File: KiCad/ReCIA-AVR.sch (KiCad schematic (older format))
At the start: 11 parts, among them U1 AVR128DA64-I_MR, U2 74AHCT1G17, U3 TLC2932AIPWR, U5 8520_DIP

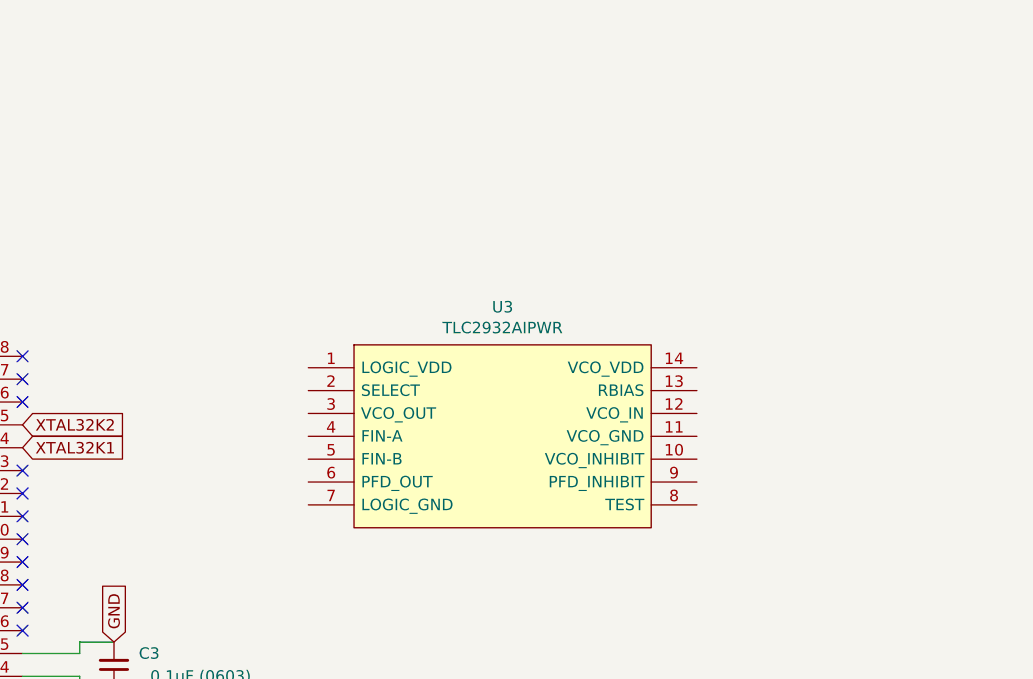
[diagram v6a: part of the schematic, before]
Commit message: Fixed placement of PLL-chip and added inductor and caps for power supply pins Logic VDD and VCO VDD for the AVR-version
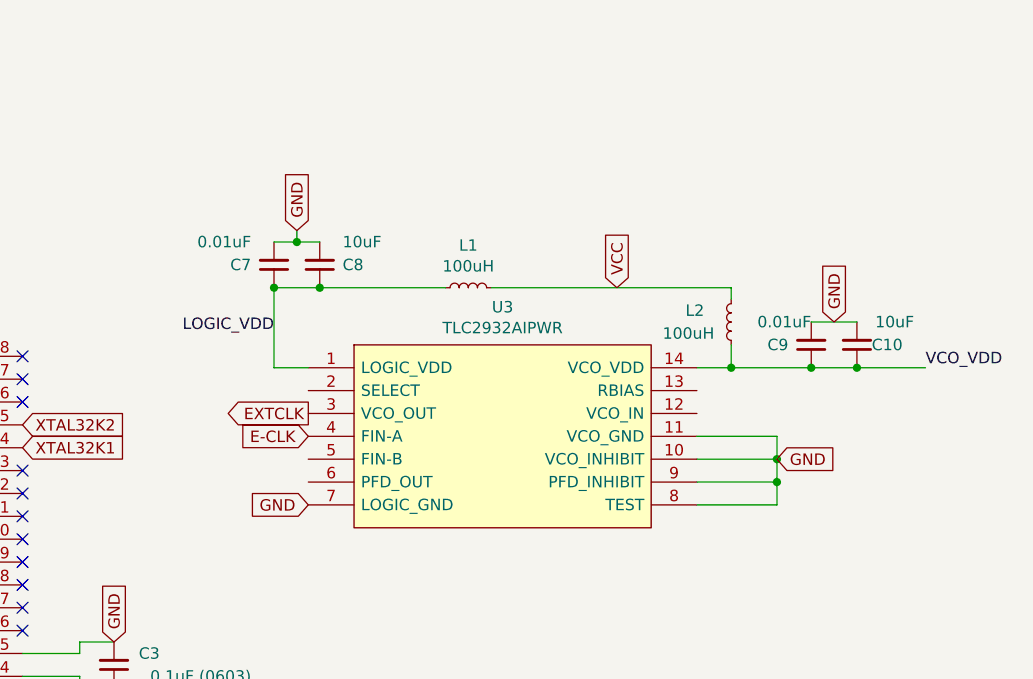
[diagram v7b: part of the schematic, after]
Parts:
- added C10, C8: 10uF, Capacitor_SMD:C_0805_2012Metric_Pad1.18x1.45mm_HandSolder, symbol Device:C_Small
- added C7, C9: 0.01uF, Capacitor_SMD:C_0603_1608Metric_Pad1.08x0.95mm_HandSolder, symbol Device:C_Small
- added L1, L2: 100uH, Inductor_SMD:L_0805_2012Metric_Pad1.15x1.40mm_HandSolder, symbol Device:L_Small
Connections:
- net E-CLK: now also U3.4 (FIN-A)
- net EXTCLK: now also U3.3 (VCO_OUT)
- net GND: now also U3.10 (VCO_INHIBIT), U3.11 (VCO_GND), U3.7 (LOGIC_GND), U3.8 (TEST), U3.9 (PFD_INHIBIT), C10.2, C7.2, C8.2, C9.2
- net VCC: now also L1.2, L2.2
- net LOGIC_VDD: now reaches U3.1 (LOGIC_VDD)
- net LOGIC_VDD: now also C7.1, C8.1, L1.1
- net VCO_VDD: now reaches U3.14 (VCO_VDD)
- net VCO_VDD: now also C10.1, C9.1, L2.1
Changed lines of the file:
@@
 Text GLabel 2050 4600 3    50   Input ~ 0
 GND
+$Comp
+L Device:L_Small L1
+U 1 1 6782C3A7
+P 8550 2350
+F 0 "L1" V 8735 2350 50  0000 C CNN
+F 1 "100uH" V 8644 2350 50  0000 C CNN
+F 2 "Inductor_SMD:L_0805_2012Metric_Pad1.15x1.40mm_HandSolder" H 8550 2350 50  0001 C CNN
+F 3 "~" H 8550 2350 50  0001 C CNN
+	1    8550 2350
+	0    -1   -1   0
+$EndComp
+$Comp
+L Device:L_Small L2
+U 1 1 6782D183
+P 9700 2500
+F 0 "L2" H 9900 2450 50  0000 R CNN
+F 1 "100uH" H 10000 2550 50  0000 R CNN
+F 2 "Inductor_SMD:L_0805_2012Metric_Pad1.15x1.40mm_HandSolder" H 9700 2500 50  0001 C CNN
+F 3 "~" H 9700 2500 50  0001 C CNN
+	1    9700 2500
+	-1   0    0    1
+$EndComp
+Wire Wire Line
+	9550 2700 9700 2700
+$Comp
+L Device:C_Small C8
+U 1 1 67831839
+P 7900 2250
+F 0 "C8" H 7800 2250 50  0000 R CNN
+F 1 "10uF" H 7800 2150 50  0000 R CNN
+F 2 "Capacitor_SMD:C_0805_2012Metric_Pad1.18x1.45mm_HandSolder" H 7900 2250 50  0001 C CNN
+F 3 "~" H 7900 2250 50  0001 C CNN
+	1    7900 2250
+	-1   0    0    1
+$EndComp
+$Comp
+L Device:C_Small C10
+U 1 1 67833368
+P 10250 2600
+F 0 "C10" H 10050 2600 50  0000 L CNN
+F 1 "10uF" H 10000 2500 50  0000 L CNN
+F 2 "Capacitor_SMD:C_0805_2012Metric_Pad1.18x1.45mm_HandSolder" H 10250 2600 50  0001 C CNN
+F 3 "~" H 10250 2600 50  0001 C CNN
+	1    10250 2600
+	-1   0    0    1
+$EndComp
+Wire Wire Line
+	9700 2350 9700 2400
+Wire Wire Line
+	9700 2600 9700 2700
+$Comp
+L Device:C_Small C7
+U 1 1 67838FC9
+P 7700 2250
+F 0 "C7" H 7800 2250 50  0000 L CNN
+F 1 "0.01uF" H 7800 2150 50  0000 L CNN
+F 2 "Capacitor_SMD:C_0603_1608Metric_Pad1.08x0.95mm_HandSolder" H 7700 2250 50  0001 C CNN
+F 3 "~" H 7700 2250 50  0001 C CNN
+	1    7700 2250
+	-1   0    0    1
+$EndComp
+Wire Wire Line
+	7900 2350 7700 2350
+Connection ~ 7900 2350
+$Comp
+L Device:C_Small C9
+U 1 1 6783A777
+P 10050 2600
+F 0 "C9" H 10150 2600 50  0000 L CNN
+F 1 "0.01uF" H 10050 2500 50  0000 L CNN
+F 2 "Capacitor_SMD:C_0603_1608Metric_Pad1.08x0.95mm_HandSolder" H 10050 2600 50  0001 C CNN
+F 3 "~" H 10050 2600 50  0001 C CNN
+	1    10050 2600
+	-1   0    0    1
+$EndComp
+Text GLabel 7800 2100 1    50   Input ~ 0
+GND
+Wire Wire Line
+	7900 2350 8450 2350
+Wire Wire Line
+	8650 2350 9700 2350
+Wire Wire Line
+	7700 2150 7800 2150
+Wire Wire Line
+	7800 2100 7800 2150
+Connection ~ 7800 2150
+Wire Wire Line
+	7800 2150 7900 2150
+Wire Wire Line
+	7700 2350 7700 2700
+Wire Wire Line
+	7700 2700 7850 2700
+Connection ~ 9700 2700
+Connection ~ 7700 2350
+Connection ~ 10050 2700
+Wire Wire Line
+	9700 2700 10050 2700
+Wire Wire Line
+	10050 2700 10250 2700
+Wire Wire Line
+	10250 2500 10050 2500
+Text GLabel 10150 2500 1    50   Input ~ 0
+GND
+Text GLabel 9200 2350 1    50   Input ~ 0
+VCC
+Text GLabel 9900 3100 2    50   Input ~ 0
+GND
+Wire Wire Line
+	9550 3000 9900 3000
+Wire Wire Line
+	9900 3000 9900 3100
+Wire Wire Line
+	9550 3100 9900 3100
+Wire Wire Line
+	9550 3200 9900 3200
+Wire Wire Line
+	9900 3200 9900 3100
+Connection ~ 9900 3100
+Text Label 7700 2550 2    50   ~ 0
+LOGIC_VDD
+Text Label 10550 2700 0    50   ~ 0
+VCO_VDD
+Wire Wire Line
+	10550 2700 10250 2700
+Connection ~ 10250 2700
+Text GLabel 7850 3300 0    50   Input ~ 0
+GND
+Wire Wire Line
+	9550 3300 9900 3300
+Wire Wire Line
+	9900 3300 9900 3200
+Connection ~ 9900 3200
+Text GLabel 7850 3000 0    50   Input ~ 0
+E-CLK
+Text GLabel 7850 2900 0    50   Output ~ 0
+EXTCLK
 $EndSCHEMATC

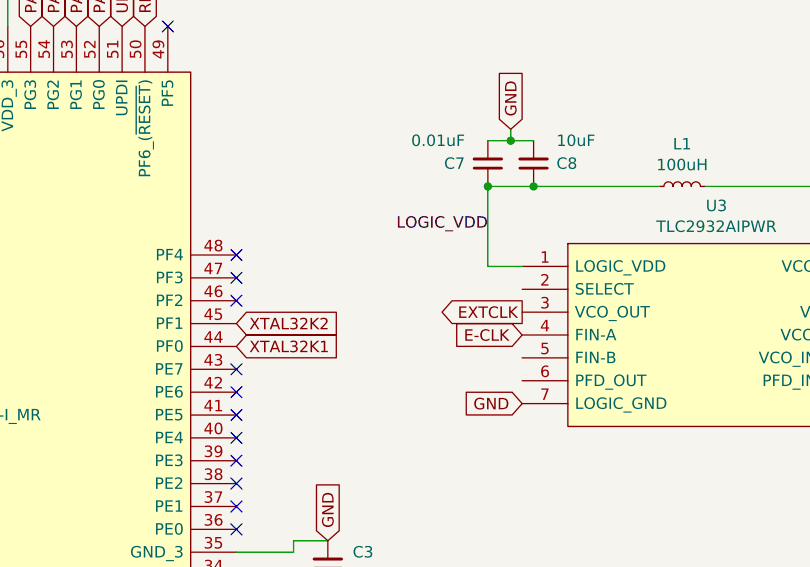
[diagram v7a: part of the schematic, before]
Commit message: Add 33 Ohm damping resistor on EXTCLK-line
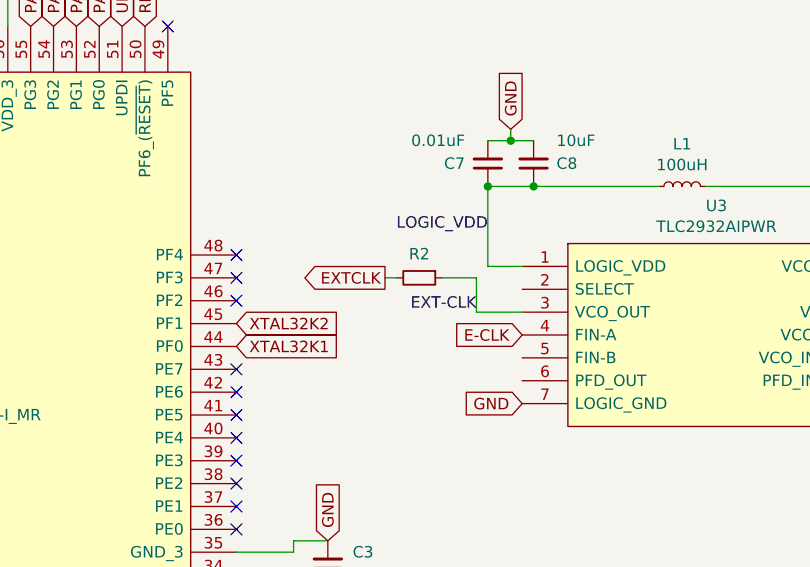
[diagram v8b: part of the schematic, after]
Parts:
- added R2: 33, Resistor_SMD:R_0603_1608Metric_Pad0.98x0.95mm_HandSolder, symbol Device:R_Small
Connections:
- net EXTCLK: now also R2.2; no longer U3.3 (VCO_OUT)
- new net EXT-CLK: R2.1, U3.3 (VCO_OUT)
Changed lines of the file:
@@
 Text GLabel 7850 3000 0    50   Input ~ 0
 E-CLK
-Text GLabel 7850 2900 0    50   Output ~ 0
+Text GLabel 7250 2750 0    50   Output ~ 0
 EXTCLK
+$Comp
+L Device:R_Small R2
+U 1 1 678932BF
+P 7400 2750
+F 0 "R2" V 7296 2750 50  0000 C CNN
+F 1 "33" V 7295 2750 50  0001 C CNN
+F 2 "Resistor_SMD:R_0603_1608Metric_Pad0.98x0.95mm_HandSolder" H 7400 2750 50  0001 C CNN
+F 3 "~" H 7400 2750 50  0001 C CNN
+	1    7400 2750
+	0    1    1    0
+$EndComp
+Wire Wire Line
+	7300 2750 7250 2750
+Wire Wire Line
+	7650 2900 7650 2750
+Wire Wire Line
+	7650 2750 7500 2750
+Wire Wire Line
+	7650 2900 7850 2900
+Text Label 7650 2900 2    50   ~ 0
+EXT-CLK
 $EndSCHEMATC
